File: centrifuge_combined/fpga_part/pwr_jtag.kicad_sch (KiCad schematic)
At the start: 72 parts, among them J1 FPGA JTAG, SW1 SW_MEC_5E, U1 XC7A100T-FTG256, U15 D5V0FS4U10LP

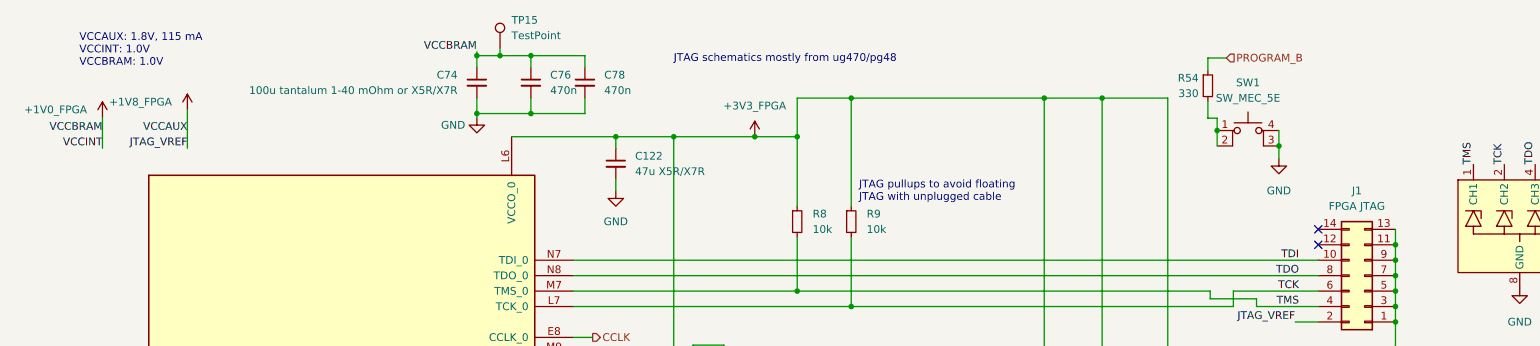
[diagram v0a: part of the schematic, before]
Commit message: Fixed Elprint complaints and JTAG VREF problems+config flash CS
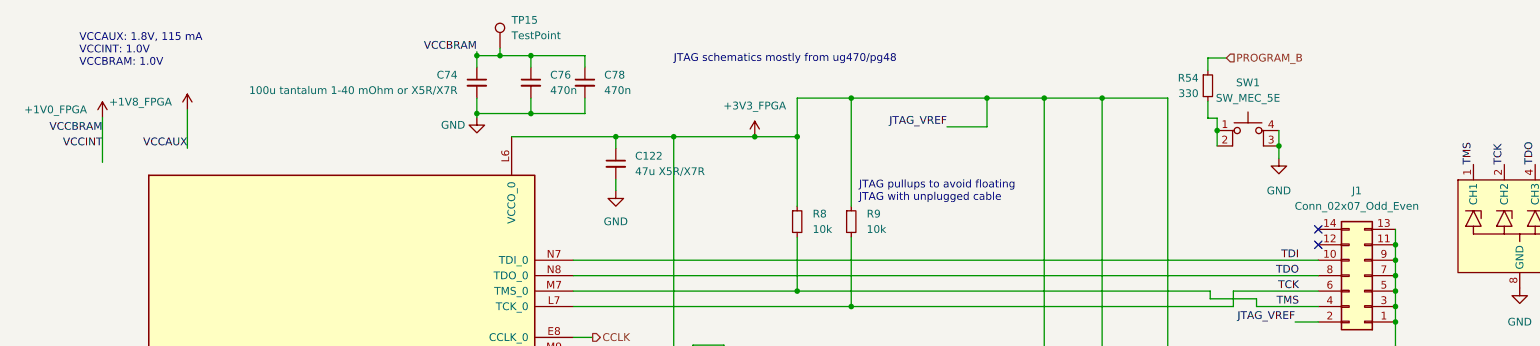
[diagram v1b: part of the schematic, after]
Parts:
- J1: value FPGA JTAG -> Conn_02x07_Odd_Even; Order Page BOUGHT https://www.digikey.no/en/products/detail/molex/0878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 -> https://www.digikey.no/en/products/detail/molex/0878311411/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
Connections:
- net +1V8_FPGA: no longer J1.2 (Pin_2)
- net +3V3_FPGA: now also J1.2 (Pin_2)
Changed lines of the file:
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@@
   (title_block
     (title "VGA Centrifuge")
-    (date "2022-10-03")
-    (rev "R3")
+    (date "2022-10-05")
+    (rev "R4")
     (comment 1 "Author: Paolo Celati")
     (comment 2 "FPGA Power & JTAG")
@@
   )
   (junction (at 39.878 150.495) (diameter 0) (color 0 0 0 0)
+  )
+  (junction (at 170.9166 26.67) (diameter 0) (color 0 0 0 0)
   )
   (junction (at 274.32 121.92) (diameter 0) (color 0 0 0 0)
@@
     (stroke (width 0) (type default) (color 0 0 0 0))
   )
+  (wire (pts (xy 170.9166 31.3944) (xy 170.9166 26.67))
+    (stroke (width 0) (type default) (color 0 0 0 0))
+  )
   (wire (pts (xy 223.52 134.62) (xy 223.52 137.16))
     (stroke (width 0) (type default) (color 0 0 0 0))
@@
     (stroke (width 0) (type default) (color 0 0 0 0))
   )
-  (wire (pts (xy 25.4 29.845) (xy 25.4 34.925))
-    (stroke (width 0) (type default) (color 0 0 0 0))
-  )
   (wire (pts (xy 223.52 101.6) (xy 217.17 101.6))
     (stroke (width 0) (type default) (color 0 0 0 0))
@@
     (stroke (width 0) (type default) (color 0 0 0 0))
   )
-  (wire (pts (xy 148.59 26.67) (xy 180.34 26.67))
+  (wire (pts (xy 148.59 26.67) (xy 170.9166 26.67))
     (stroke (width 0) (type default) (color 0 0 0 0))
   )
@@
     (stroke (width 0) (type default) (color 0 0 0 0))
   )
+  (wire (pts (xy 170.9166 26.67) (xy 180.34 26.67))
+    (stroke (width 0) (type default) (color 0 0 0 0))
+  )
   (wire (pts (xy 159.3596 188.5188) (xy 159.3596 185.9788))
     (stroke (width 0) (type default) (color 0 0 0 0))
@@
     (stroke (width 0) (type default) (color 0 0 0 0))
   )
+  (wire (pts (xy 25.4 29.845) (xy 25.4 37.2364))
+    (stroke (width 0) (type default) (color 0 0 0 0))
+  )
   (wire (pts (xy 274.32 137.16) (xy 274.32 139.7))
     (stroke (width 0) (type default) (color 0 0 0 0))
@@
   )
   (wire (pts (xy 188.722 141.986) (xy 197.612 141.986))
+    (stroke (width 0) (type default) (color 0 0 0 0))
+  )
+  (wire (pts (xy 164.338 31.3944) (xy 170.9166 31.3944))
     (stroke (width 0) (type default) (color 0 0 0 0))
   )
@@
     (effects (font (size 1.27 1.27)) (justify right bottom))
   )
-  (label "VCCAUX" (at 39.37 32.385 180)
+  (label "VCCAUX" (at 39.37 34.925 180)
     (effects (font (size 1.27 1.27)) (justify right bottom))
   )
@@
     (effects (font (size 1.27 1.27)) (justify right bottom))
   )
-  (label "JTAG_VREF" (at 39.37 34.925 180)
+  (label "JTAG_VREF" (at 164.338 31.3944 180)
     (effects (font (size 1.27 1.27)) (justify right bottom))
   )
@@
     (in_bom yes) (on_board yes) (fields_autoplaced)
     (property "Reference" "J1" (id 0) (at 231.775 41.91 0))
-    (property "Value" "FPGA JTAG" (id 1) (at 231.775 44.45 0))
+    (property "Value" "Conn_02x07_Odd_Even" (id 1) (at 231.775 44.45 0))
     (property "Footprint" "centrifuge footprints:878311411" (id 2) (at 233.045 55.88 0)
       (effects (font (size 1.27 1.27)) hide)
@@
       (effects (font (size 1.27 1.27)) hide)
     )
-    (property "Order Page" "BOUGHT https://www.digikey.no/en/products/detail/molex/0878311411/3313107" (id 4) (at 233.045 55.88 0)
-      (effects (font (size 1.27 1.27)) hide)
-    )
+    (property "Order Page" "https://www.digikey.no/en/products/detail/molex/0878311411/3313107" (id 4) (at 233.045 55.88 0)
+      (effects (font (size 1.27 1.27)) hide)
+    )
